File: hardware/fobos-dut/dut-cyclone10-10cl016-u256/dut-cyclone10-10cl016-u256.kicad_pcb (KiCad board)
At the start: 6 copper layers, 88.9 x 76.2 mm, 178 parts, among them J1 Target, J10 Barrel_Jack_Switch, J2 Pmod 2x6, J3 575-8, J4 Glitch, J5 Conn_01x02, J6 Measure, J7 0878321420, J8 575-8, J9 Measure, Q1 FDS9435A, Q2 MMBT3904, Q3 BSS138, Q4 BSS138, Q5 BSS138, Q6 BSS138, Q7 BSS138, Q8 MMBT3904, SW1 SW_DIP_x03, SW2 SW_DIP_x03, U1 10CL016YU256I7G, U10 SP3003-04ATG, U11 SP3003-04ATG, U12 MAX8560EZK+T, U2 SP3003-04ATG, U3 SP3003-04ATG, U4 SP3003-04ATG, U5 INA225, U6 BGA2801, U7 TS3A5018DBQR, U8 LTC3569EFE#PBF

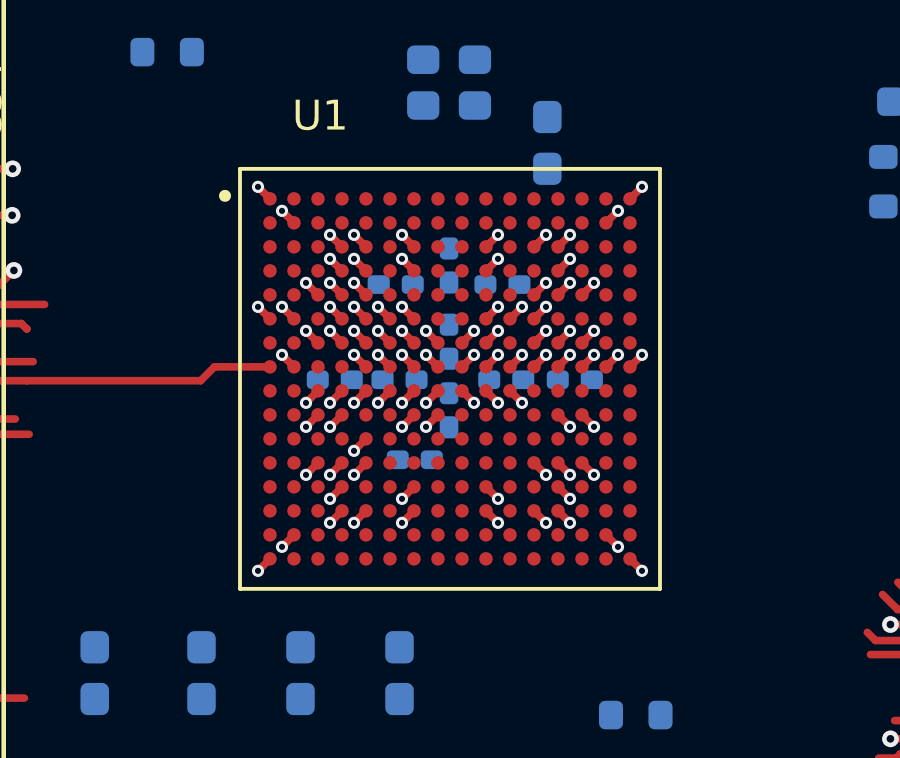
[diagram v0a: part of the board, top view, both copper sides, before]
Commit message: Changed BGA pad diameter from 0.45mm to 0.38mm Changed BGA vias from 8/16mil to 10/18mil
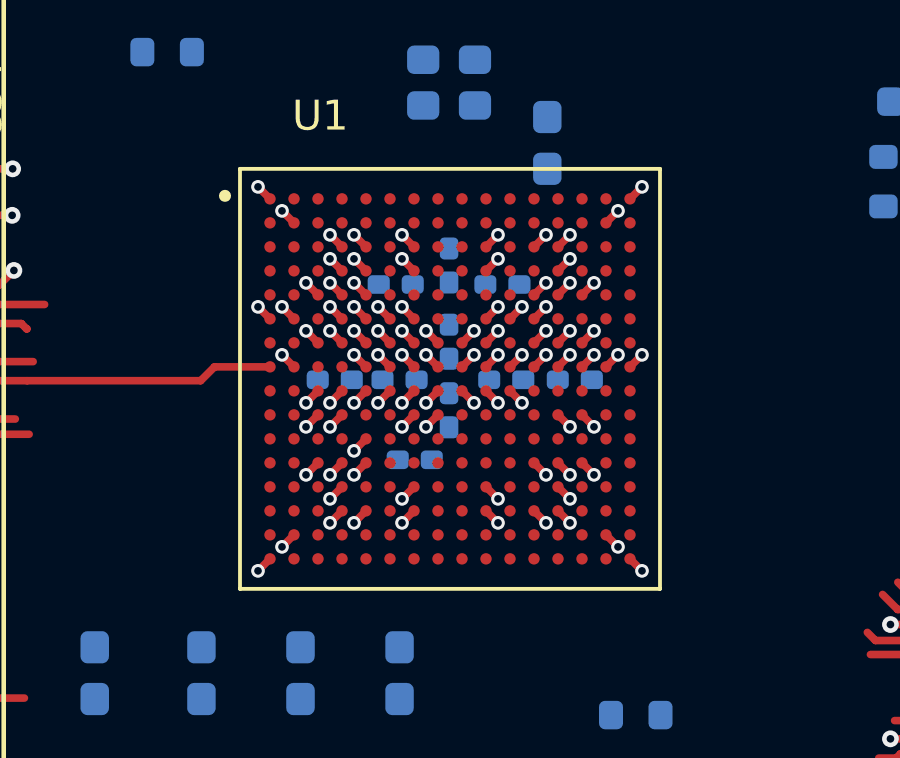
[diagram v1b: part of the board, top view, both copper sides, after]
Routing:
- removed copper zone on In4.Cu, net GND
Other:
- copper layers 6 -> 4

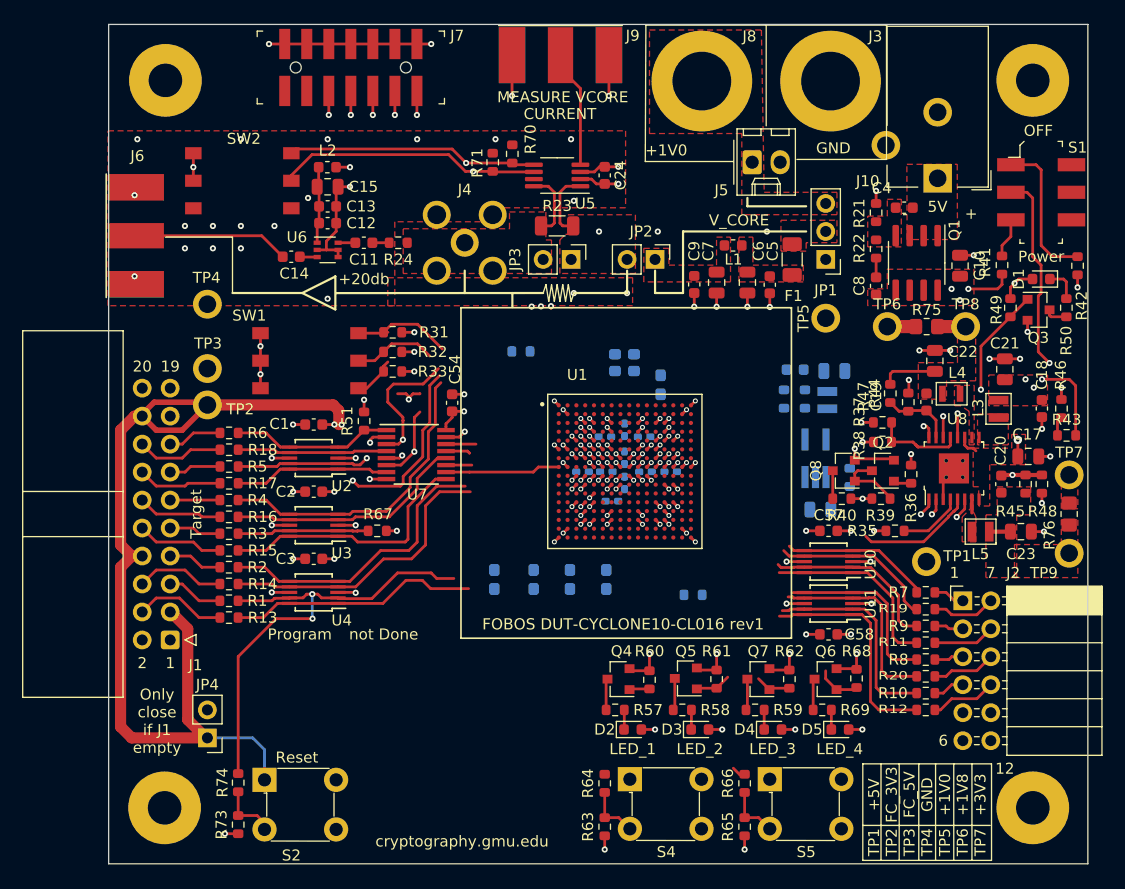
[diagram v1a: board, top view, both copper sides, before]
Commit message: Updated jtag connector to match terasic usb blaster Connected SPI Flash Layout is in work
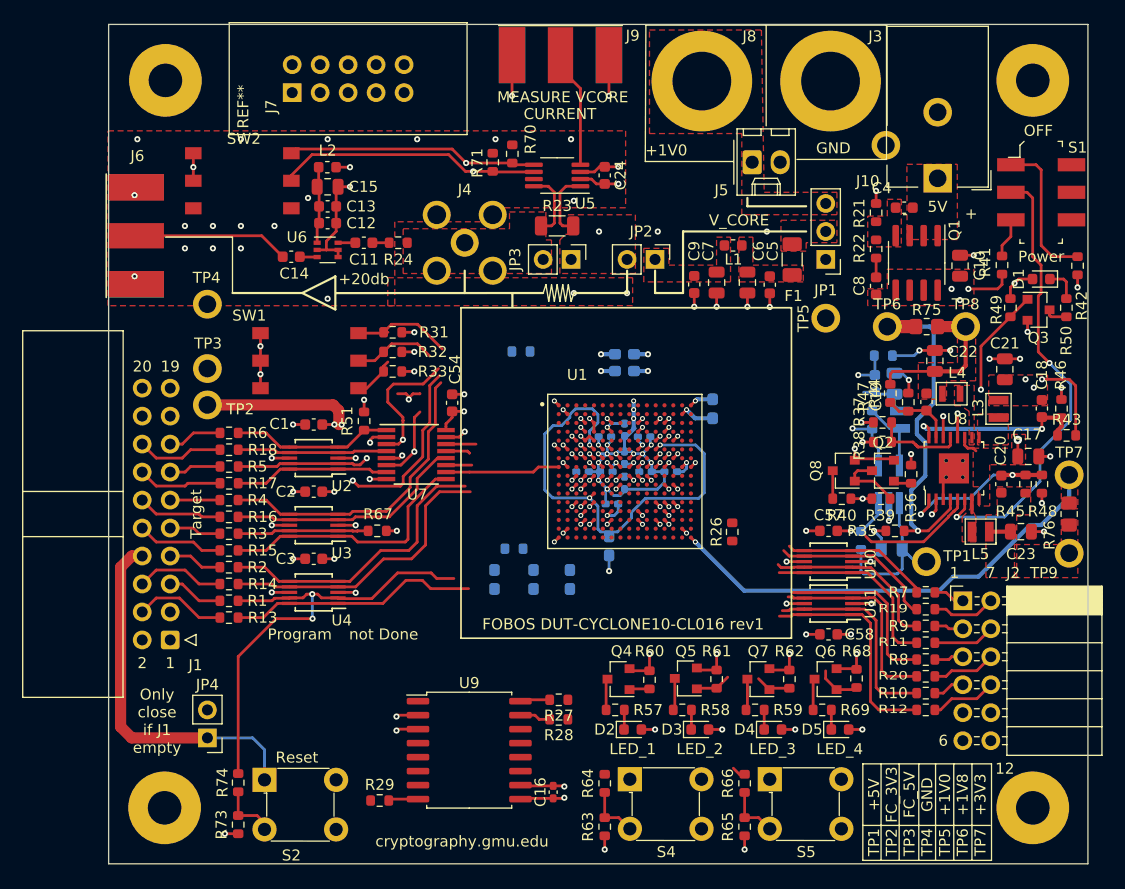
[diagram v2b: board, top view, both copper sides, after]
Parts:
- added C16: .1uF, Capacitor_SMD:C_0402_1005Metric_Pad0.74x0.62mm_HandSolder, F.Cu at (143.4, 140.9)
- added R27: 20R, Resistor_SMD:R_0603_1608Metric, F.Cu at (143.9, 132.5)
- added R28: 20R, Resistor_SMD:R_0603_1608Metric, F.Cu at (143.9, 134.3)
- added R29: 20R, Resistor_SMD:R_0603_1608Metric, F.Cu at (127.6, 141.6)
- added R52: 4.7KR, Resistor_SMD:R_0603_1608Metric, B.Cu at (139.8, 118.8)
- added U9: MX25L51245GMI-08G, Package_SO:SOIC-16W_7.5x10.3mm_P1.27mm, F.Cu at (135.7, 137.1)
- J7: value 0878321420 -> Conn_02x05_Odd_Even; footprint cerg:PinHeader_2x7_P2mm_SMD -> Connector_PinHeader_2.54mm:PinHeader_2x05_P.54mm_Vertical_Shrouded
- R26: moved to F.Cu
- moved R34 9.84 mm to (173.3, 101.2), turned to 180 degrees
- moved C63 7.39 mm to (174.1, 118.8)
- moved C64 7.35 mm to (172.6, 103.8), turned to 270 degrees
- moved U12 7.07 mm to (173.8, 112.9)
- moved L6 6.84 mm to (174.8, 107.9)
- moved R26 6.73 mm to (159.6, 117.3), turned to 90 degrees
- moved R30 6.39 mm to (172.3, 107.1), turned to 90 degrees
- moved R77 5.80 mm to (171.3, 118.0)
- moved J7 5.79 mm to (119.7, 77.4), turned to 90 degrees
- moved C65 5.58 mm to (174.3, 103.8), turned to 90 degrees
- moved C56 5.21 mm to (157.8, 106.1), turned to 270 degrees
- moved C40 3.06 mm to (148.4, 118.5)
- moved C41 0.25 mm to (148.7, 114.7)
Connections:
- J7 pad 1: GND -> /FPGA Programming/TCK
- J7 pad 10: /FPGA Programming/TDI -> GND
- J7 pad 2: +3V3 -> GND
- J7 pad 3: GND -> /FPGA Programming/TDO
- J7 pad 4: /FPGA Programming/TMS -> +3V3
- J7 pad 5: GND -> /FPGA Programming/TMS
- J7 pad 6: /FPGA Programming/TCK -> Net-(J7-Pad6)
- J7 pad 7: GND -> Net-(J7-Pad7)
- J7 pad 8: /FPGA Programming/TDO -> Net-(J7-Pad8)
- J7 pad 9: GND -> /FPGA Programming/TDI
- U1 pad C1: Net-(U1-PadC1) -> ASDO
- U1 pad F4: SW_nCONFIG -> SW_nSTATUS
- U1 pad H5: SW_nSTATUS -> SW_nCONFIG
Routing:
- net FC_3V3: track 124.0 -> 364.9 mm
- net +3V3: track 19.6 -> 160.5 mm, vias 25 -> 27
- net FC_5V: track 0.00 -> 119.7 mm
- net +5V: track 14.4 -> 88.7 mm
- net VCCINT: track 12.4 -> 69.8 mm, vias 11 -> 16
- net +1V2_PLL: track 10.7 -> 59.1 mm, vias 4 -> 5
- net +2V5_PLL: track 1.70 -> 47.6 mm
- net +1V2: track 7.80 -> 33.6 mm
- net ON_OFF: track 19.9 -> 41.6 mm
- net GND: track 136.1 -> 152.2 mm, vias 115 -> 116
- net Net-(C64-Pad1): track 0.00 -> 13.7 mm, vias 0 -> 2
- net /Power1/FB1: track 4.22 -> 16.9 mm
- net /Power1/FB3: track 5.37 -> 15.2 mm
- net Net-(L6-Pad1): track 0.00 -> 6.59 mm
- net /Power1/pre1V2PLL: track 7.63 -> 14.2 mm
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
